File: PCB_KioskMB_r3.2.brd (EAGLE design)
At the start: 146.1 x 101.9 mm, 339 parts, among them IC1 ISL60002DIH325Z-TK, IC18 FT232RL, IC19 MCP6022-I/ST, IC2 SN65HVD12D, IC20 LTC1771EMS8, IC21 LTC1771EMS8, IC3 PIC24FJ256GA110-I/PT, IC4 PIC10F200T-I/OT, IC5 LM75ADP, IC6 24LC32A-I/MS, IC7 PCF2123TS/1-T, IC8 M25P16-VMN6P, IC9 LM3405AXMK/NOPB, J1 DF11-10DP-2DSA(01), J10 CCM03-3504LFT-NR, J13 3-641215-3, J14 3-641215-2, J15 3-641215-4, J16 3-641215-4, J40 DNP, J43 3-641215-4, J44 3-641215-4, J45 3-641215-4, J46 3-641215-5, J47 DF11-10DP-2DSA(01), J48 3-641215-2, J49 3-641215-2, J5 3-641215-2, J6 3-641215-2, J7 SS-6566-NF, J8 TSW-108-07-G-D, J9 SS-6566-NF, Q1 SSM6P49NU,LFPZ, Q14 TSM9938HEUK+T, Q15 SI4564DY, Q16 CSD87331Q3D, Q17 TSM9938HEUK+T, Q18 SI4564DY, Q19 CSD87331Q3D, Q2 FDC6330L, Q20 IPD30N06S2L-23, Q21 IPD30N06S2L-23, Q22 FDN352AP, Q23 FDN352AP, Q24 BSS138, Q3 SR3.3.TCT, Q4 7B-28.63636MAAJ-T, Q5 FDC6324L, Q6 CM519 32.768KDZF-UT, Q7 SSM6P49NU,LFPZ, Q8 IPD30N06S2L-23, Q9 IPD30N06S2L-23, U1 LTC1955, U2 HRXL-MAXSONAR-WRC-MB7387, U3 ADS1015, U6 TPS43061, U7 TPS43061, U8 TPA3111D1PWP, U9 OPA322SAIDBVT, X1 FH12-10S-0.5S1.00MM

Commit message: added BOM to csv
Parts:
- moved H1 42.7 mm to (-126.9, 20.9)
- moved F3 25.5 mm to (-112.8, 61.5)
- moved D32 16.1 mm to (-105.3, 78.5)
- moved J50 13.0 mm to (-79.3, 69.4)
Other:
- board size 146.1 x 101.9 mm -> 147.4 x 102.5 mm
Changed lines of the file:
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@@
 <setting verticaltext="up"/>
 </settings>
-<grid distance="1" unitdist="mil" unit="mil" style="lines" multiple="1" display="yes" altdistance="0.025" altunitdist="inch" altunit="inch"/>
+<grid distance="0.1" unitdist="mm" unit="mm" style="lines" multiple="1" display="yes" altdistance="0.025" altunitdist="inch" altunit="inch"/>
 <layers>
 <layer number="1" name="Top" color="4" fill="1" visible="yes" active="yes"/>
@@
 <text x="108.4" y="47.4" size="1.016" layer="125" ratio="12">Prog</text>
 <rectangle x1="100.4" y1="47.4" x2="101.4" y2="48.4" layer="125" rot="R90"/>
-<wire x1="146.05" y1="101.9" x2="0" y2="101.9" width="0" layer="20"/>
-<wire x1="0" y1="101.9" x2="0" y2="0" width="0" layer="20"/>
-<wire x1="0" y1="0" x2="146.05" y2="0" width="0" layer="20"/>
-<wire x1="146.05" y1="0" x2="146.05" y2="101.9" width="0" layer="20"/>
+<wire x1="146.8" y1="102.5" x2="-0.6" y2="102.5" width="0" layer="20"/>
+<wire x1="-0.6" y1="102.5" x2="-0.6" y2="0" width="0" layer="20"/>
+<wire x1="-0.6" y1="0" x2="146.8" y2="0" width="0" layer="20"/>
+<wire x1="146.8" y1="0" x2="146.8" y2="102.5" width="0" layer="20"/>
 <text x="139.700003125" y="59.700003125" size="0.762" layer="125" ratio="12">B1</text>
 <text x="112.07950625" y="27.273196875" size="0.762" layer="125" ratio="12">C1</text>
@@
 </element>
 <element name="C187" library="DISCRETE" package="ES-7,5" value="2mF/16V" x="-90.207" y="48.6556"/>
-<element name="J50" library="CON-PhoenixContac-AON" package="TERM-2" value="" x="-68.1368" y="76.0148"/>
-<element name="D32" library="Littelfuse" package="SMB" value="P6SMB16A" x="-89.203" y="78.5008"/>
-<element name="F3" library="Littelfuse" package="1812" value="2920L250DR" x="-89.5208" y="71.9434" rot="R180"/>
+<element name="J50" library="CON-PhoenixContac-AON" package="TERM-2" value="" x="-79.3368" y="69.4148"/>
+<element name="D32" library="Littelfuse" package="SMB" value="P6SMB16A" x="-105.303" y="78.5008"/>
+<element name="F3" library="Littelfuse" package="1812" value="2920L250DR" x="-112.8208" y="61.5434" rot="R180"/>
 <element name="U2" library="elocktech_lib" package="HRXL-MAXSONAR-WRC-MB7387" value="HRXL-MAXSONAR-WRC-MB7387" x="94.5" y="95.5"/>
 <element name="C35" library="DISCRETE" package="0603" value="0.1uF" x="110.6" y="93.7" rot="R180"/>
 <element name="R26" library="DISCRETE" package="0603-0RTOP" value="10K" x="107" y="93.7"/>
-<element name="H1" library="SparkFun-Hardware" package="STANDOFF-ELECTRICAL" value="STANDOFF_ELECTRICAL" x="-85.0746" y="29.5264"/>
+<element name="H1" library="SparkFun-Hardware" package="STANDOFF-ELECTRICAL" value="STANDOFF_ELECTRICAL" x="-126.8746" y="20.9264"/>
 <element name="H2" library="SparkFun-Hardware" package="STANDOFF-ELECTRICAL" value="STANDOFF_ELECTRICAL" x="65.528" y="27.21"/>
 <element name="H3" library="SparkFun-Hardware" package="STANDOFF-ELECTRICAL" value="STANDOFF_ELECTRICAL" x="142.715" y="20.4705"/>
@@
 <contactref element="J40" pad="S4"/>
 <polygon width="0.5" layer="2">
-<vertex x="46.566" y="101.6"/>
+<vertex x="46.566" y="102.1"/>
 <vertex x="46.566" y="74.419896875"/>
 <vertex x="45.72" y="74.422"/>
@@
 <vertex x="17.272" y="74.422"/>
 <vertex x="17.272" y="65.042"/>
-<vertex x="0.4" y="65.042"/>
-<vertex x="0.4" y="0.4"/>
-<vertex x="144.15" y="0.3"/>
-<vertex x="145.75" y="0.3"/>
-<vertex x="145.75" y="101.6"/>
+<vertex x="-0.2" y="65.042"/>
+<vertex x="-0.2" y="0.4"/>
+<vertex x="146.35" y="0.4"/>
+<vertex x="146.35" y="102.1"/>
 </polygon>
 <contactref element="U2" pad="7"/>
@@
 <wire x1="89.535" y1="38.989" x2="89.2556" y2="39.2684" width="0.3556" layer="1"/>
 <wire x1="89.2556" y1="39.2684" x2="88.5952" y2="39.2684" width="0.3556" layer="1"/>
-<wire x1="3.278" y1="92.7185" x2="0.762" y2="90.2025" width="1.016" layer="2"/>
-<wire x1="0.762" y1="90.2025" x2="0.762" y2="64.008" width="1.016" layer="2"/>
 <wire x1="66.948" y1="42.038" x2="67.817" y2="42.038" width="0.1524" layer="1"/>
 <wire x1="67.817" y1="42.038" x2="67.818" y2="42.037" width="0.1524" layer="1"/>
@@
 <wire x1="27.591" y1="34.5374" x2="27.5844" y2="34.544" width="0.3556" layer="1"/>
 <via x="27.5844" y="34.544" extent="1-16" drill="0.3"/>
-<wire x1="-86.397" y1="48.6556" x2="-85.0746" y2="29.5264" width="0" layer="19" extent="1-1"/>
-<wire x1="-87.003" y1="78.5008" x2="-86.397" y2="48.6556" width="0" layer="19" extent="1-1"/>
-<wire x1="-70.6768" y1="79.8248" x2="-87.003" y2="78.5008" width="0" layer="19" extent="1-1"/>
-<wire x1="0.762" y1="90.2025" x2="-70.6768" y2="79.8248" width="0" layer="19" extent="1-2"/>
+<wire x1="3.278" y1="92.7185" x2="0.154" y2="89.5945" width="1" layer="2"/>
+<wire x1="0.154" y1="89.5945" x2="0.154" y2="64.3" width="1" layer="2"/>
+<wire x1="-86.397" y1="48.6556" x2="-126.8746" y2="20.9264" width="0" layer="19" extent="1-1"/>
+<wire x1="-103.103" y1="78.5008" x2="-86.397" y2="48.6556" width="0" layer="19" extent="1-1"/>
+<wire x1="-81.8768" y1="73.2248" x2="-103.103" y2="78.5008" width="0" layer="19" extent="1-1"/>
+<wire x1="0.154" y1="89.5945" x2="-81.8768" y2="73.2248" width="0" layer="19" extent="1-2"/>
 </signal>
 <signal name="N$1">
@@
 <wire x1="48.50145625" y1="63.2968" x2="45.50665625" y2="66.2916" width="1.27" layer="15"/>
 <wire x1="45.50665625" y1="66.2916" x2="39.1266" y2="66.2916" width="1.27" layer="15"/>
-<wire x1="-65.5968" y1="79.8248" x2="23.178" y2="78.816" width="0" layer="19" extent="1-1"/>
+<wire x1="-76.7968" y1="73.2248" x2="23.178" y2="78.816" width="0" layer="19" extent="1-1"/>
 </signal>
 <signal name="B12_L">
@@
 <wire x1="55.9054" y1="88.6504" x2="55.905" y2="88.65" width="1.27" layer="15"/>
 <wire x1="60.8076" y1="63.9064" x2="60.8076" y2="72.2376" width="1.27" layer="15"/>
-<wire x1="-91.756" y1="71.9434" x2="-94.017" y2="48.6556" width="0" layer="19" extent="1-1"/>
-<wire x1="-91.403" y1="78.5008" x2="-91.756" y2="71.9434" width="0" layer="19" extent="1-1"/>
+<wire x1="-115.056" y1="61.5434" x2="-94.017" y2="48.6556" width="0" layer="19" extent="1-1"/>
+<wire x1="-107.503" y1="78.5008" x2="-115.056" y2="61.5434" width="0" layer="19" extent="1-1"/>
 <wire x1="5.234" y1="8.448" x2="-94.017" y2="48.6556" width="0" layer="19" extent="1-1"/>
 </signal>
@@
 <contactref element="C172" pad="2"/>
 <polygon width="0.5" layer="2" isolate="0.254" rank="2">
-<vertex x="0.4" y="101.6"/>
-<vertex x="45.666" y="101.6"/>
+<vertex x="-0.2" y="102.1"/>
+<vertex x="45.666" y="102.1"/>
 <vertex x="45.666" y="75.438"/>
 <vertex x="41.91" y="75.438"/>
@@
 <vertex x="16.002" y="75.438"/>
 <vertex x="16.002" y="66.04"/>
-<vertex x="0.4" y="66.04"/>
+<vertex x="-0.2" y="66.04"/>
 </polygon>
 <polygon width="0.5" layer="1">
@@
 <contactref element="J45" pad="4"/>
 <contactref element="F3" pad="1"/>
-<wire x1="-87.2856" y1="71.9434" x2="5.334" y2="53.848" width="0" layer="19" extent="1-1"/>
+<wire x1="-110.5856" y1="61.5434" x2="5.334" y2="53.848" width="0" layer="19" extent="1-1"/>
 </signal>
 <signal name="N$9">

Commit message: cleaned up silk
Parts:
- removed F1, F2: (no value), technol:REF
- added FID1, FID2, FID3: (no value), technol:REF
- moved TP5 0.20 mm to (101.5, 46.5)
- moved TP61 0.13 mm to (29.5, 75.8)
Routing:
- net N$7: track 51.6 -> 52.4 mm

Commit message: added components ( for sbc power) and updated lan components.
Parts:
- removed H1: STANDOFF_ELECTRICAL, SparkFun-Hardware:STANDOFF-ELECTRICAL
- moved D32 132.4 mm to (8.27, 10.4), turned to 270 degrees
- moved F3 127.2 mm to (3.74, 10.7), turned to 90 degrees
- moved C187 100.0 mm to (8.91, 35.2), turned to 90 degrees
- moved J50 78.8 mm to (-3.00, 50.0), turned to 270 degrees
- moved J45 46.9 mm to (4.62, 3.16), turned to 0 degrees
- moved R36 39.0 mm to (11.6, 54.3), turned to 0 degrees
- moved R35 33.5 mm to (13.2, 52.3), turned to 0 degrees
- moved JP5 33.3 mm to (-5.27, 40.1)
- moved C37 31.0 mm to (8.16, 54.8), turned to 180 degrees
- moved R31 22.4 mm to (6.83, 51.3), turned to 270 degrees
- moved U3 21.6 mm to (9.92, 50.0), turned to 0 degrees
- moved R32 17.6 mm to (8.18, 45.7), turned to 180 degrees
- moved JP2 16.0 mm to (-5.27, 29.4)
- moved JP3 15.8 mm to (-5.27, 18.6)
- moved JP4 15.6 mm to (-5.27, 7.89)
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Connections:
- net +3.3V/2: no longer Q3.4
- net DGND: no longer H1.P1
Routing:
- net P12V: track 120.4 -> 170.0 mm
- net BAT_SENSE: track 21.0 -> 61.5 mm, vias 0 -> 2
- net 18V_GND: track 39.4 -> 76.4 mm, vias 0 -> 1
- net BAT_GND: track 35.4 -> 70.4 mm, vias 0 -> 1
- net 18V_SENSE: track 30.1 -> 59.8 mm, vias 0 -> 1
- net DGND: track 402.9 -> 427.3 mm, vias 141 -> 140
- net SDA1: track 201.6 -> 224.9 mm, vias 6 -> 8
- net SMB_SDA: track 117.5 -> 140.7 mm, vias 2 -> 5
- net +5V: track 96.8 -> 75.2 mm
- net SMB_SCL: track 123.2 -> 144.2 mm, vias 2 -> 3
- net SCL1: track 191.5 -> 205.2 mm
- net +3.3V/2: track 201.1 -> 187.9 mm, vias 7 -> 9
- net MIC_AMP_EN: track 20.7 -> 33.5 mm
- net +SMB: track 470.9 -> 481.2 mm, vias 6 -> 9
- net MICROPHONE: track 23.6 -> 32.9 mm
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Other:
- board size 147.4 x 102.5 mm -> 157 x 103 mm
- board text added: "HOPT"
- board text added: "HORZ"
- board text added: "SBC VCC"
- board text added: "SIM CARD"
- board text added: "VERT"
- board text added: "VIN"

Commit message: ADDED SILK
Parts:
- moved J6 10.1 mm to (147.1, 4.00)
- moved C114 10.0 mm to (136.3, 82.1)
- moved R152 10.0 mm to (131.1, 91.2)
- moved R22 10.0 mm to (130.3, 67.3)
- moved C129 10.0 mm to (68.4, 64.7)
- moved C132 10.0 mm to (68.2, 56.1)
- moved C133 10.0 mm to (68.7, 50.3)
- moved C138 10.0 mm to (67.2, 39.6)
- moved R165 10.0 mm to (68.2, 54.2)
- moved R171 10.0 mm to (64.7, 42.7)
- moved R176 10.0 mm to (73.1, 18.0)
- moved C154 10.0 mm to (39.3, 69.8)
- moved C182 10.0 mm to (38.7, 85.6)
- moved D6 10.0 mm to (40.9, 8.96)
- moved R179 10.0 mm to (39.7, 36.9)
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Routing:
- net N$67: track 24.6 -> 23.9 mm
- net DGND: track 427.3 -> 427.9 mm
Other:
- board text added: "+SMB"
- board text added: "BAT RETURN"
- board text added: "BAT SENSE"
- board text added: "BTN 1/2"
- board text added: "MIC"
- board text added: "MIC EN"
- board text added: "SBC AUD IN"
- board text added: "SPKR"
- board text removed: "T01 0.016in T02 0.020in T03 0.032in T04 0.035in T05 0.036in T06 0.040in T07 0.056in T08 0.062in T09 0.065in T10 0.075in T11 0.091in T12 0.126in T13 0.128in T14 0.138in"

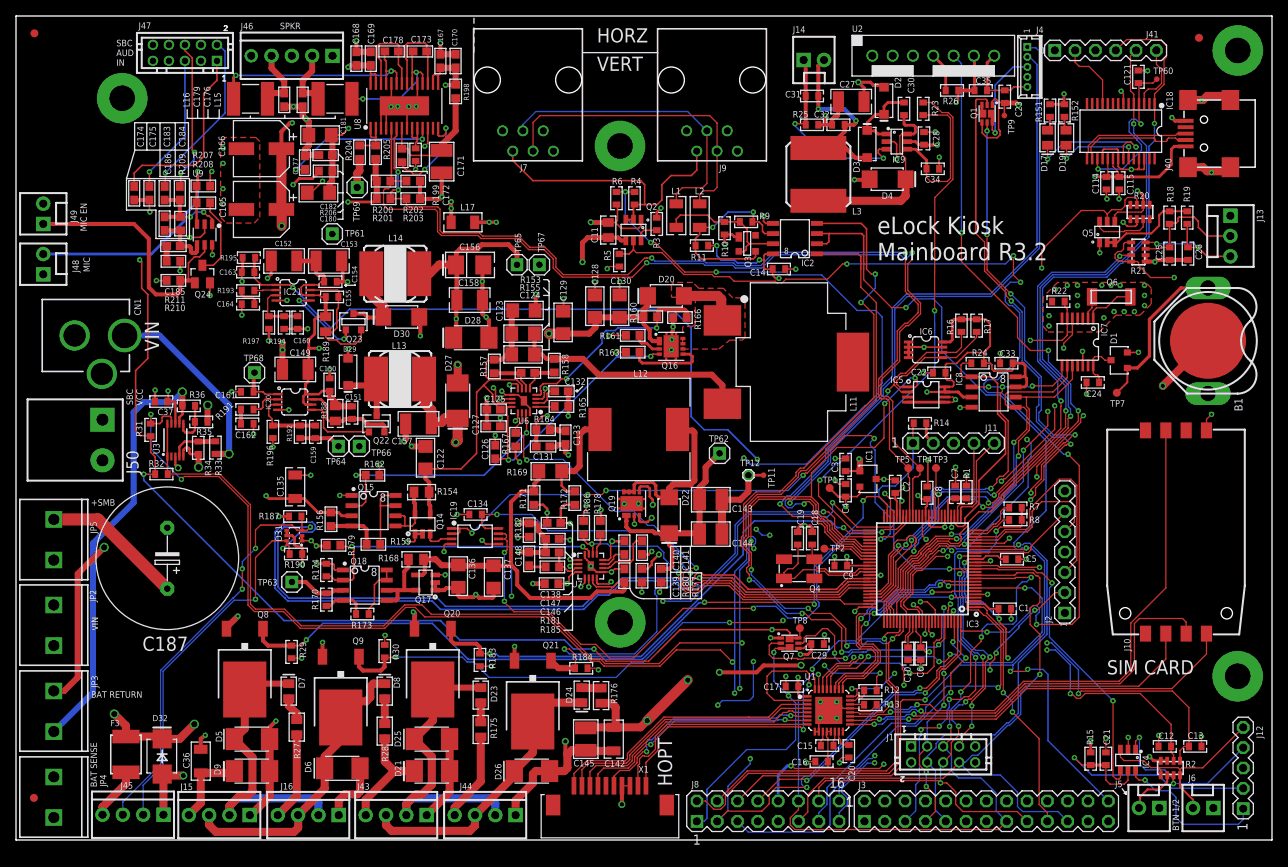
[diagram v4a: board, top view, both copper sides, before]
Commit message: update connectors
USB B connector, VREF design, connectors.
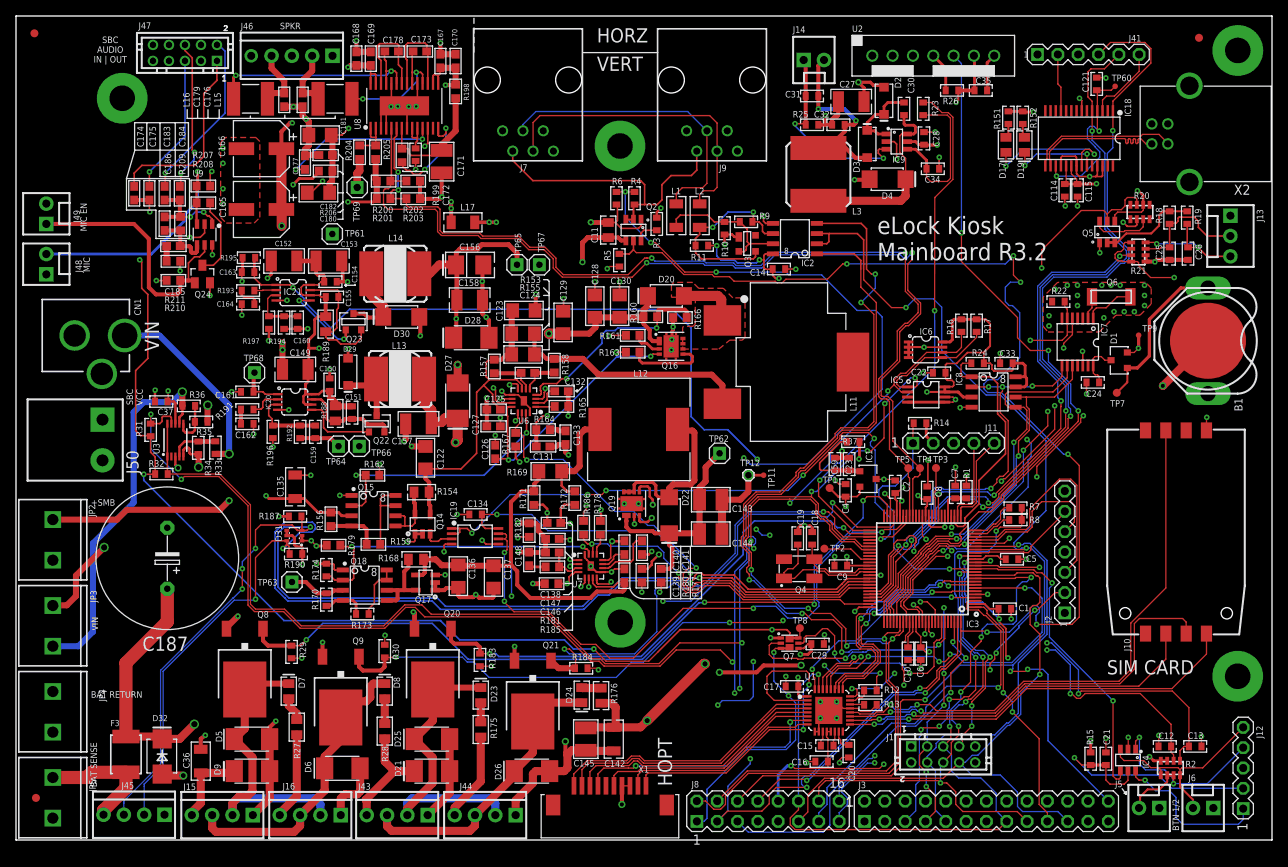
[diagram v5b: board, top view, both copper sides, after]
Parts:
- removed C3: 1u/10V, DISCRETE:0603
- removed J4: (no value), con-molex-AOM:53047-05
- removed J40: DNP, CON-Hirose-AON:UX60
- removed Q1: SSM6P49NU,LFPZ, Toshiba-AON:MICRO_FET
- added C59: 10uF/4V, DISCRETE:0603
- added DRILEGEND: (no value), drilegend:DRILEGEND
- added R37: 300R, DISCRETE:0603
- added X2: MINI-USB_4P-85-32004-10X, con-cypressindustries:85-32004-10X
- C23: value 10uF/10V -> 10uF/4V
- moved C23 49.9 mm to (104.1, 47.0), turned to 90 degrees
- moved JP5 32.3 mm to (4.60, 7.81)
- moved TP9 32.2 mm to (140.3, 63.1), turned to 90 degrees
- moved JP2 10.7 mm to (4.60, 40.1)
- moved JP4 10.7 mm to (4.60, 18.6)
- moved JP3 10.7 mm to (4.60, 29.3)
- moved C121 5.28 mm to (135.1, 94.5)
- moved C114 5.28 mm to (131.1, 81.2)
- moved R151 5.28 mm to (124.0, 90.3)
- moved R152 5.28 mm to (125.8, 90.3)
- moved D19 5.28 mm to (126.0, 86.9)
- moved C115 5.28 mm to (132.7, 81.2)
- moved D17 5.28 mm to (123.7, 86.9)
- moved IC18 5.28 mm to (132.9, 87.7)
- moved TP60 5.28 mm to (137.4, 94.2)
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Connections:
- removed net +3.3V/7: Q1.3, Q1.P2
- removed net /3.3V/7_ON: IC3.96, Q1.5
- removed net /MH_PWR: IC3.97, Q1.2
- removed net MH_DATA: IC3.59, J4.2
- removed net MH_STROBE: IC3.58, J4.1
- removed net N$5: J4.3, Q1.6, Q1.P1
- removed net N$54: F3.1, J45.4
- new net +SMB_PRE: F3.1, J45.4, JP5.P2
- new net N$39: C23.1, C59.1, IC1.1, R37.1
- net +3.3V: now also R37.2; no longer C23.2, C3.1, IC1.1, Q1.1, Q1.4
- net +SMB: no longer JP5.P2
- net DGND: now also C23.2, C59.2, X2.4; no longer C23.1, C3.2, J4.4, J4.5, J40.5, J40.S1, J40.S2, J40.S3, J40.S4
- net SBC_5V_VBUS: now also X2.1; no longer J40.1
- net SBC_USB_B_D_N: now also X2.2; no longer J40.2
- net SBC_USB_B_D_P: now also X2.3; no longer J40.3
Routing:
- net MH_STROBE: track 92.9 -> 0.00 mm, vias 1 -> 0
- net MH_DATA: track 90.5 -> 0.00 mm, vias 1 -> 0
- net /MH_PWR: track 80.2 -> 0.00 mm, vias 4 -> 0
- net /3.3V/7_ON: track 76.9 -> 0.00 mm, vias 6 -> 0
- net +3.3V: track 482.5 -> 420.5 mm, vias 27 -> 26
- net DGND: track 427.9 -> 402.4 mm, vias 140 -> 137
- net +SMB: track 481.2 -> 463.5 mm, vias 9 -> 8
- net +SMB_PRE: track 0.00 -> 15.9 mm
- net N$5: track 13.5 -> 0.00 mm, vias 1 -> 0
- net 18V_GND: track 76.4 -> 63.0 mm
- net BAT_SENSE: track 61.5 -> 50.6 mm
- net N$39: track 0.00 -> 10.4 mm
- net BAT_GND: track 70.4 -> 61.2 mm
- net SBC_5V_VBUS: track 41.1 -> 49.0 mm
- net N$54: track 6.52 -> 0.00 mm
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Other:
- board text added: "01-16"
- board text added: "01-20"
- board text added: "LAYER-STACK"
- board text added: "SBC AUDIO IN | OUT"
- board text removed: "SBC AUD IN"
